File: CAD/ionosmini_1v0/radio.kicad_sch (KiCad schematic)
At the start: 24 parts, among them CON1 TFC-120-02-F-D-A-K-TR, CON2 TFC-120-02-F-D-A-K-TR, IC1 ESP32-S3-DEVKITC-1-N8R2

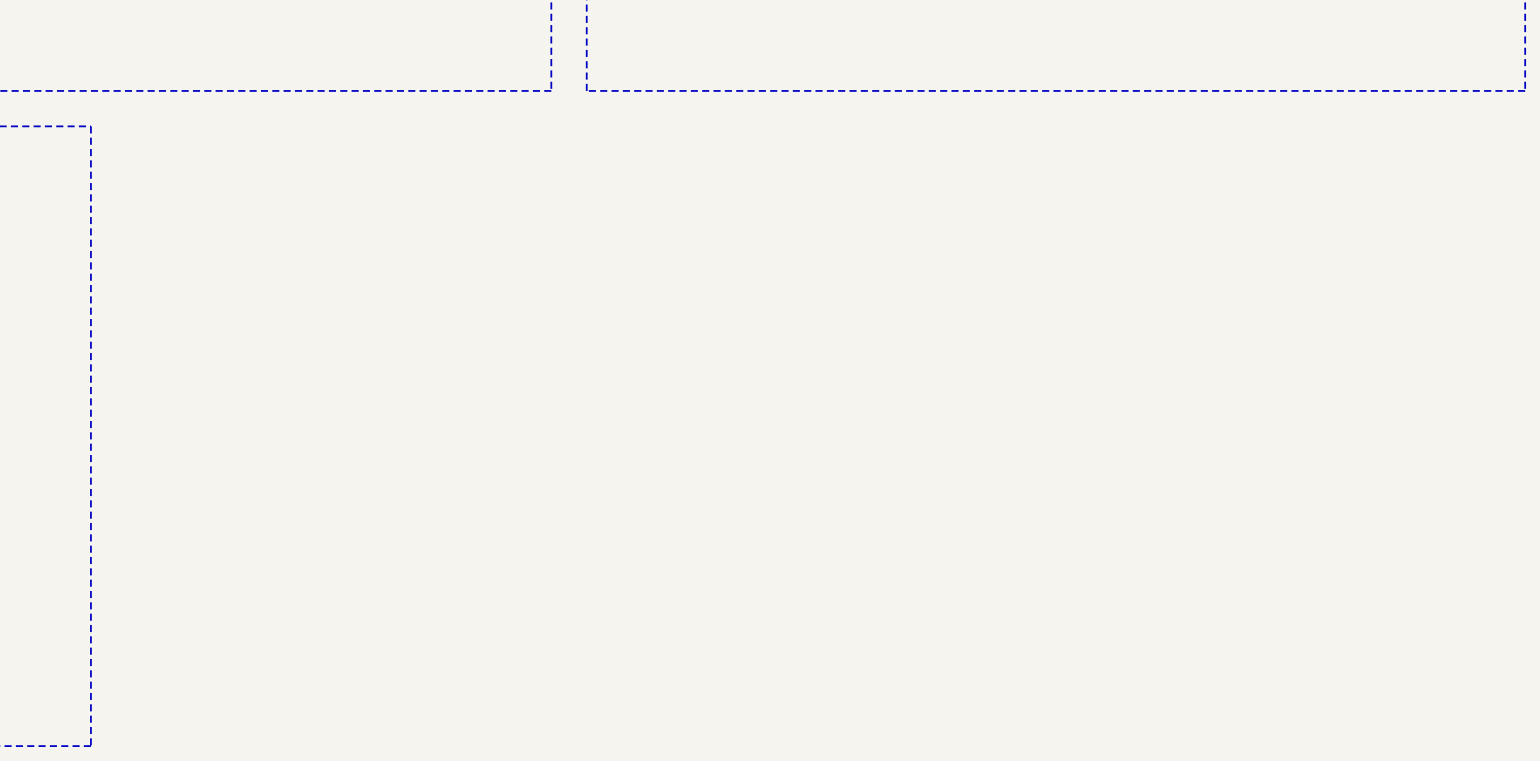
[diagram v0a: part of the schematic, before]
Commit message: SWD debug header CON3 (1x6 2.54 mm, not fitted) for an external debugger
Flashing the FG23 so far went only through the ESP32's bit-banged SWD.
CON3 adds a row of six plated holes on the right board edge, outside
the radio board's outline, for a J-Link / Simplicity Link with a pogo
clip or solder-in pins. Pin order follows the Tag-Connect TC2030-CTX:
1 VTref (VMCU_IN), 2 SWDIO, 3 nRESET, 4 SWCLK, 5 GND, 6 SWO.

The pins are on the radio side of the solder-jumper cut points
(SWDIO_RB, SWCLK_RB, SWO_RB, RESETn_RB): with JP2 and JP6-JP8 cut the
ESP32 is off the bus entirely; uncut, firmware keeps its SWD pins as
inputs while a debugger is attached. VTref only senses VMCU.

Schematic: radio sheet, new block with KiCad's TC2030 symbol (VCC top,
GND bottom) on a 1x6 header footprint; lint clean, ERC 0 errors.
twin_check asserts every CON3 pin reaches its radio-board pin.
twin_3d resolves KiCad's own ${KICADnn_3DMODEL_DIR} from the install.

PCB: TP8 moves 2 mm down to make room; full re-route (0/45/90). On two
layers the SWD nets are routed first (after the power pass RESETn_RB
had no way to the edge), and a net a pass cannot route is re-routed
together with its neighbours. The GND pads of C1 and R9 ended up
walled in by tracks; each got a GND via next to the pad and the nets in
the way were re-routed around it. GND pockets stitched, tracks centred
in their channels. DRC 0 errors, 0 unconnected, schematic parity 0.
3D reference images recaptured. README: SWD header section.
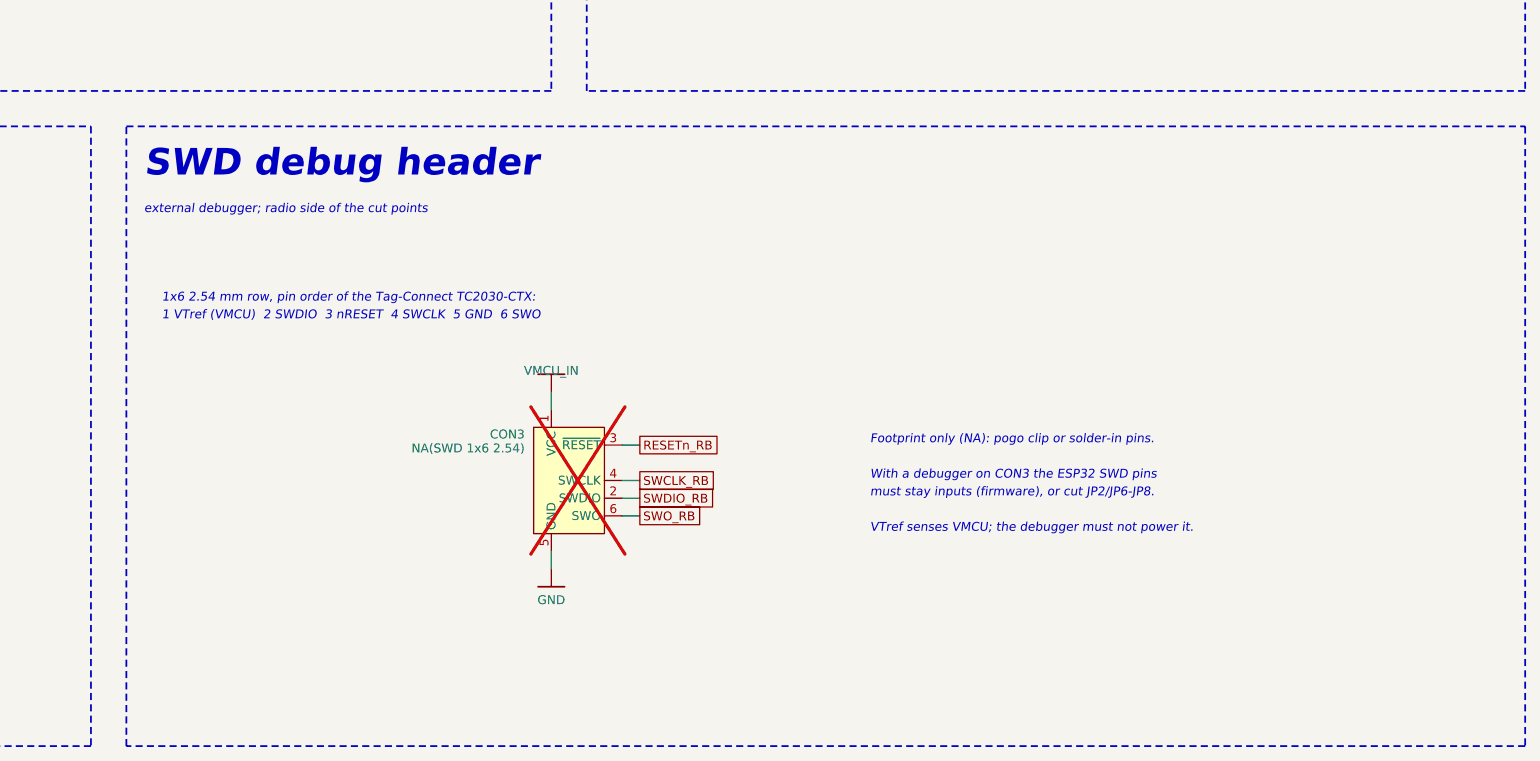
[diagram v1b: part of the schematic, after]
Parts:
- added CON3: NA(SWD 1x6 2.54), Connector_PinHeader_2.54mm:PinHeader_1x06_P2.54mm_Vertical, symbol Connector:Conn_ARM_SWD_TagConnect_TC2030
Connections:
- net GND: now also CON3.5 (GND)
- net RESETn_RB: now also CON3.3 (~{RESET})
- net SWCLK_RB: now also CON3.4 (SWCLK)
- net SWDIO_RB: now also CON3.2 (SWDIO)
- net SWO_RB: now also CON3.6 (SWO)
- net VMCU_IN: now also CON3.1 (VCC)
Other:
- note added: "1 VTref (VMCU) 2 SWDIO 3 nRESET 4 SWCLK 5 GND 6 SWO"
- note added: "1x6 2.54 mm row, pin order of the Tag-Connect TC2030-CTX:"
- note added: "Footprint only (NA): pogo clip or solder-in pins."
- note added: "SWD debug header"
- note added: "VTref senses VMCU; the debugger must not power it."
- note added: "With a debugger on CON3 the ESP32 SWD pins"
- note added: "external debugger; radio side of the cut points"
- note added: "must stay inputs (firmware), or cut JP2/JP6-JP8."
